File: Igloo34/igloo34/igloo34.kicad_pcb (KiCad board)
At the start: 4 copper layers, 82 x 100 mm, 56 parts, among them J1 Conn_01x08_Pin, J10 Conn_01x10, J11 LSHM-120-02.5-L-DV-A-S-TR, J12 LSHM-120-02.5-L-DV-A-S-TR, J13 Conn_01x10, J14 Conn_01x10, J15 LSHM-120-02.5-L-DV-A-S-TR, J16 Conn_01x02, J17 Conn_01x02, J18 Conn_01x02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

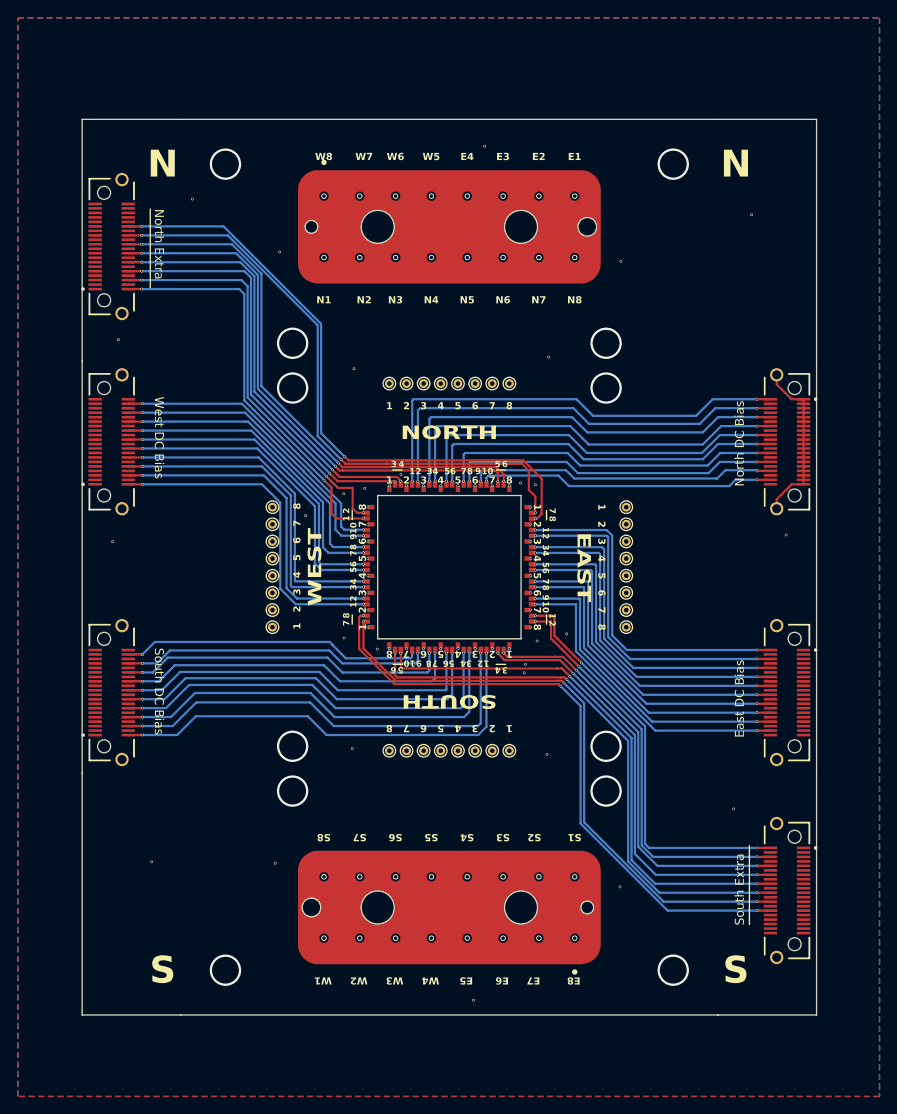
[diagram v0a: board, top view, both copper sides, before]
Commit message: increased via sizes
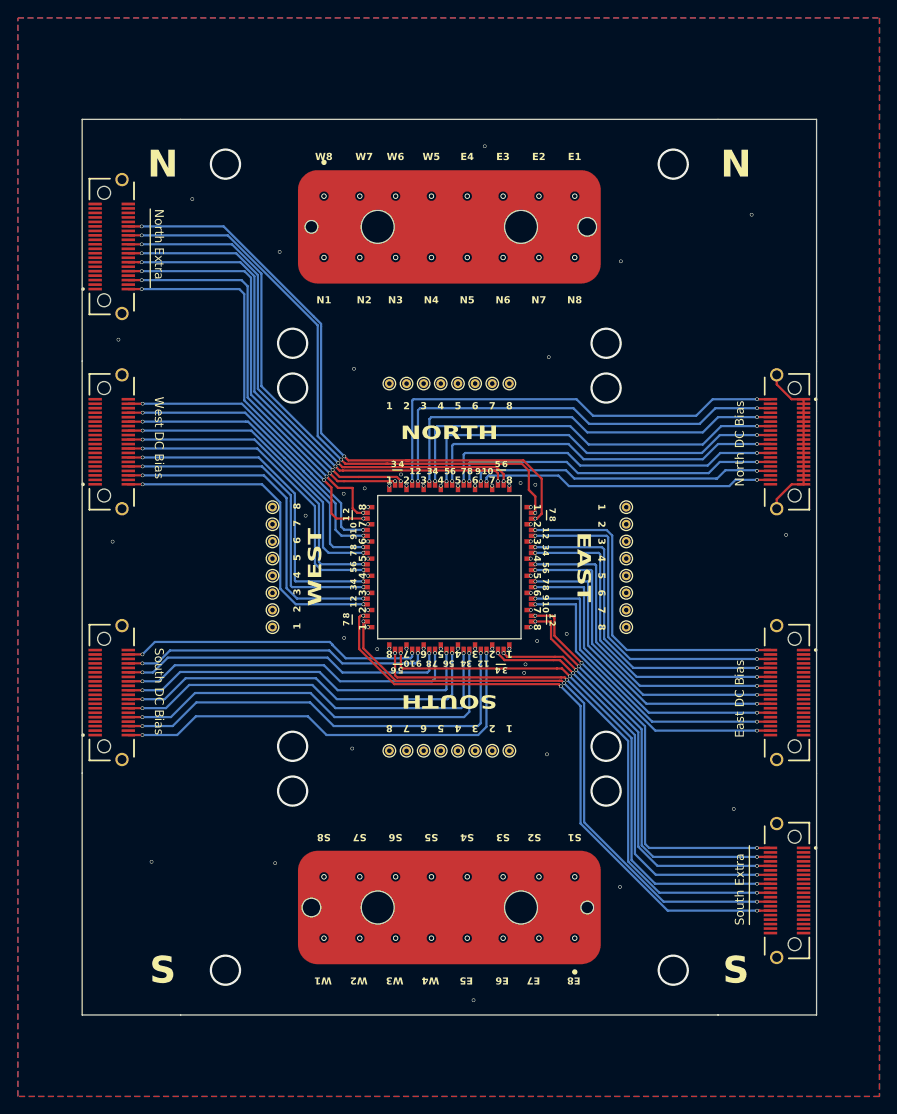
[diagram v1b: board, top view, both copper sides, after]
